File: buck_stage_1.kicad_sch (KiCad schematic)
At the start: 30 parts

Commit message: SH-RPi v2 schematic design
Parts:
- removed C301, C308, C311, C316: (no value), symbol Device:C
- removed R301, R305, R306, R308, R309, R312, R313: (no value), symbol Device:R
- removed U302: (no value), symbol SH-RPi:LMR14050SDDA
- removed U303: (no value), symbol SH-RPi:GS8052
- added C302: 4.7nF, symbol Device:C_Small
- added C304: 100nF, Capacitor_SMD:C_0402_1005Metric, symbol Device:C
- added C305: 100nF, Capacitor_SMD:C_0402_1005Metric, symbol Device:C_Small
- added D301, D304: BZT52C3V3S, Diode_SMD:D_SOD-323, symbol Device:D_Zener
- added D302: 1N4148WT, Diode_SMD:D_SOD-523, symbol Device:D_Small
- added Q301, Q302: MMBT5551, Package_TO_SOT_SMD:SOT-23, symbol Transistor_BJT:MMBT5551L
- added Q303: LBSS84LT1G, Package_TO_SOT_SMD:SOT-23, symbol Transistor_FET:BSS84
- added R302: 576k, Resistor_SMD:R_0402_1005Metric, symbol Device:R
- added R303: 91k, Resistor_SMD:R_0402_1005Metric, symbol Device:R
- added R304: 100k, symbol Device:R
- added R306: 10k, symbol Device:R_Small
- added R309: 18k, symbol Device:R_Small
- added R311: 2k, symbol Device:R
- added U301: RT6365, symbol SH-RPi:RT6365
- added U302, U303: COS1333TRD, Package_TO_SOT_SMD:SOT-23-5, symbol SH-RPi:COS1333
- C301: renamed from C314; value (none) -> 10uF/50V; footprint (none) -> Capacitor_SMD:C_1206_3216Metric; LCSC C13585 -> (none)
- C303: renamed from C304; value (none) -> 100nF; footprint (none) -> Capacitor_SMD:C_0603_1608Metric; LCSC C1525 -> (none)
- C306: value (none) -> 47n; LCSC C15195 -> (none)
- C307: renamed from C305; value (none) -> 47uF/10V; footprint (none) -> Capacitor_SMD:C_0805_2012Metric; LCSC C16780 -> (none); Notes Min 6.3V -> Min 10V
- C308: renamed from C307; value (none) -> 100nF; footprint (none) -> Capacitor_SMD:C_0402_1005Metric
- D303: renamed from D301; value (none) -> SS56; footprint (none) -> Diode_SMD:D_SMA; LCSC C22452 -> C65009
- D305: renamed from D302; value (none) -> 1N4148WT; footprint (none) -> Diode_SMD:D_SOD-523
- JP301: value (none) -> Bridged; footprint (none) -> Jumper:SolderJumper-2_P1.3mm_Bridged_Pad1.0x1.5mm
- L301: value (none) -> FXL0530-3R3-M; footprint (none) -> SH-RPi:L_MWSA0503S; LCSC C285700 -> C475518
- R301: renamed from R304; value (none) -> 50m; footprint (none) -> Resistor_SMD:R_1206_3216Metric; LCSC C127703 -> (none)
- R305: renamed from R311; value (none) -> 68k; footprint (none) -> Resistor_SMD:R_0402_1005Metric; LCSC C25783 -> (none)
- R307: value (none) -> 510R; LCSC C25768 -> (none)
- R308: renamed from R315; value (none) -> 5.1R; footprint (none) -> Resistor_SMD:R_0603_1608Metric
- R310: value (none) -> 100R; LCSC C25918 -> (none)
- R312: renamed from R302; value (none) -> 100k; footprint (none) -> Resistor_SMD:R_0402_1005Metric; LCSC C25774 -> (none)
- R313: renamed from R303; value (none) -> 10k; footprint (none) -> Resistor_SMD:R_0402_1005Metric; LCSC C25750 -> (none)
- R314: value (none) -> 1.1k; LCSC C25769 -> (none)
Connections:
- net EN is gone; now on an unnamed net: R314.1
- net FB: now also U301.5 (FB); no longer C306.2
- net GND: now also C306.1, R307.2, C302.1, C304.1, C305.1, D304.2 (A), Q301.2 (E), R303.1, R311.2, U301.7 (GND), U301.9 (PGND), U303.2 (V-); no longer R310.2, R314.2
- net SW: now also C303.1, U301.8 (SW); no longer R308.1
- net Vin: now also R301.2, R310.1, R310.2, C305.2, D301.1 (K), Q303.2 (S), R304.1, U302.4 (-), U302.5 (V+)
- net Vout: no longer C306.1, R301.2
- net BOOT: now reaches R308.2
- net BOOT: now also U301.1 (BOOT); no longer C303.1
- net at D305.1 (K): now also U303.4 (-); no longer JP301.1 (A)
- net at D305.2 (A): now also U303.1
- net at R307.1: now also Q302.2 (E), R306.2
- net at R305.1: now also U301.4 (RT)
- net BS: no longer names the net of C303.2
- net BS: now also R308.1, D302.1 (K)
- net REG3.3V renamed +3V3
- net +3V3: now also U303.5 (V+)
- net Vcap: no longer names the net of R301.1
- net Vcap: now also R302.1, U301.2 (VIN), U302.3 (+); no longer R307.2
- new net: JP301.1 (A), R314.2
- new net: R302.2, R303.2, U301.3 (EN)
- new net: R309.2, U301.6 (COMP)
- new net: Q303.1 (G), U302.1
- new net: C304.2, D301.2 (A), Q302.3 (C), U302.2 (V-)
- new net: Q301.3 (C), Q302.1 (B), R304.2
- new net: C302.2, R309.1
- new net: Q301.1 (B), R306.1
- new net +5V: D302.2 (A)
- new net Iin: C306.2, D304.1 (K), Q303.3 (D), R311.1, U303.3 (+)
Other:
- note added: "Buck filter design from RT6365 design tool"
- note added: "Constant current source with about 1.25mA current through the biasing zener diode"
- note added: "FB voltage divider designed to have a 8.8V voltage at Vout"
- note added: "Floating opamp with current output. Design from LMP8646."
- note added: "Max 0.8 A current input"
- note added: "Voltage follower with diode rectification"
- note added: "Zener used to protect the next stage from overvoltage"
- note added: "f_sw = 1.393 MHz"
- note removed: "Buck filter design from WEBENCH"
- note removed: "EN voltage divider set to place the UVLO start and stop limits at 8.6 and 7.9V, respectively."
- note removed: "FB voltage divider designed to have a 2.6V voltage at Vout"
- note removed: "Max ca. 3.1 A current output"
- moved on the sheet: C301, C303, C307, C308, D303, D305, JP301, L301, R301, R305, R308, R312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

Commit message: WIP: Assign footprints and LCSC part numbers
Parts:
- added C308: 22uF/16V, Capacitor_SMD:C_0805_2012Metric, symbol Device:C
- C301: LCSC (none) -> C13585
- C302: footprint (none) -> Capacitor_SMD:C_0402_1005Metric; LCSC (none) -> C1538
- C303: LCSC (none) -> C14663
- C306: value 47n -> 47nF; footprint (none) -> Capacitor_SMD:C_0603_1608Metric; LCSC (none) -> C1622
- C307: value 47uF/10V -> 22uF/16V; LCSC (none) -> C98190; Notes Min 10V -> Min 16V
- renumbered C308 to C309
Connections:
- net GND: now also C308.2
- net Vout: now also C308.1
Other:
- moved on the sheet: C307

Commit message: Assign footprints and part numbers to components
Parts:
- removed U303: COS1333TRD, Package_TO_SOT_SMD:SOT-23-5, symbol SH-RPi:COS1333
- added U303: LMV321-TR, Package_TO_SOT_SMD:SOT-23-5, symbol Amplifier_Operational:LMV321
- C306: value 47nF -> 10nF; footprint Capacitor_SMD:C_0603_1608Metric -> Capacitor_SMD:C_0402_1005Metric; LCSC C1622 -> C15195
- R301: value 50m -> 10m; LCSC (none) -> C105362
- R302: value 576k -> 510k; LCSC (none) -> C11616
- R303: value 91k -> 75k; LCSC (none) -> C25798
- R304: footprint (none) -> Resistor_SMD:R_0402_1005Metric; LCSC (none) -> C25741
- R305: LCSC (none) -> C36871
- R306: footprint (none) -> Resistor_SMD:R_0402_1005Metric; LCSC (none) -> C25744
- R307: footprint (none) -> Resistor_SMD:R_0402_1005Metric; LCSC (none) -> C25123
- R309: footprint (none) -> Resistor_SMD:R_0402_1005Metric; LCSC (none) -> C25762
- R310: footprint (none) -> Resistor_SMD:R_0402_1005Metric; LCSC (none) -> C25076
- R311: value 2k -> 10k; footprint (none) -> Resistor_SMD:R_0402_1005Metric; LCSC (none) -> C25744
- R312: LCSC (none) -> C25741
- R313: LCSC (none) -> C25744
- R314: value 1.1k -> 470R; footprint (none) -> Resistor_SMD:R_0402_1005Metric; LCSC (none) -> C25117
- U301: footprint (none) -> Package_SO:SOIC-8-1EP_3.9x4.9mm_P1.27mm_EP2.41x3.3mm_ThermalVias; LCSC (none) -> C3024482
- U302: value COS1333TRD -> COS1333TR; LCSC C5156551 -> C693072
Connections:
- net +3V3: now also U303.5 (V+)
- net GND: now also U303.2 (V-)
- net Iin: now also U303.1 (+)
- net at D305.1 (K), R314.1: now also U303.3 (-)
- net at D305.2 (A): now also U303.4
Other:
- moved on the sheet: C309, R301

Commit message: WIP: PCB layout
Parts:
- added J301: Conn_02x02_Odd_Even, Connector_PinHeader_2.54mm:PinHeader_2x02_P2.54mm_Vertical, symbol Connector_Generic:Conn_02x02_Odd_Even
- added R315: 7.5k, Resistor_SMD:R_0402_1005Metric, symbol Device:R_Small
- added R316: 3.9k, Resistor_SMD:R_0402_1005Metric, symbol Device:R_Small
- D301: LCSC C2932762 -> C188195
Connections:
- net GND: now also R315.2, R316.2
- net Iin: now also J301.1 (Pin_1), J301.3 (Pin_3)
- net Vin: no longer C301.1, Q303.2 (S), R310.2, U302.4 (-)
- net B1_VIN: now reaches R301.1, R302.1, U301.2 (VIN), U302.3 (+)
- net B1_VIN: now also C301.1
- net VF-: now reaches D305.1 (K), R314.1, U303.3 (-)
- net VFO: now reaches D305.2 (A), U303.4
- net FBB: now reaches JP301.1 (A), R314.2
- net CCSE2: now reaches Q302.2 (E), R307.1
- net CCSE2: now also R306.1; no longer R306.2
- net DAO: now reaches Q303.1 (G), U302.1
- net FVSS: now reaches C304.2, D301.2 (A), Q302.3 (C), U302.2 (V-)
- net CCSC1: now reaches Q301.3 (C), Q302.1 (B), R304.2
- net CCSB1: now reaches Q301.1 (B)
- net CCSB1: now also R306.2; no longer R306.1
- new net: J301.2 (Pin_2), R315.1
- new net: J301.4 (Pin_4), R316.1
- new net DA-: Q303.2 (S), R310.2, U302.4 (-)
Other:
- note added: "Current limit adjustment"
- note added: "Place a jumper between 1 and 2 to increase the current limit to 1.9 A."
- note added: "Place a jumper between 3 and 4 to increase the current limit to 2.9 A."
- moved on the sheet: C301, C302, C303, C304, C305, C306, C307, C308, C309, D301, D302, D303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

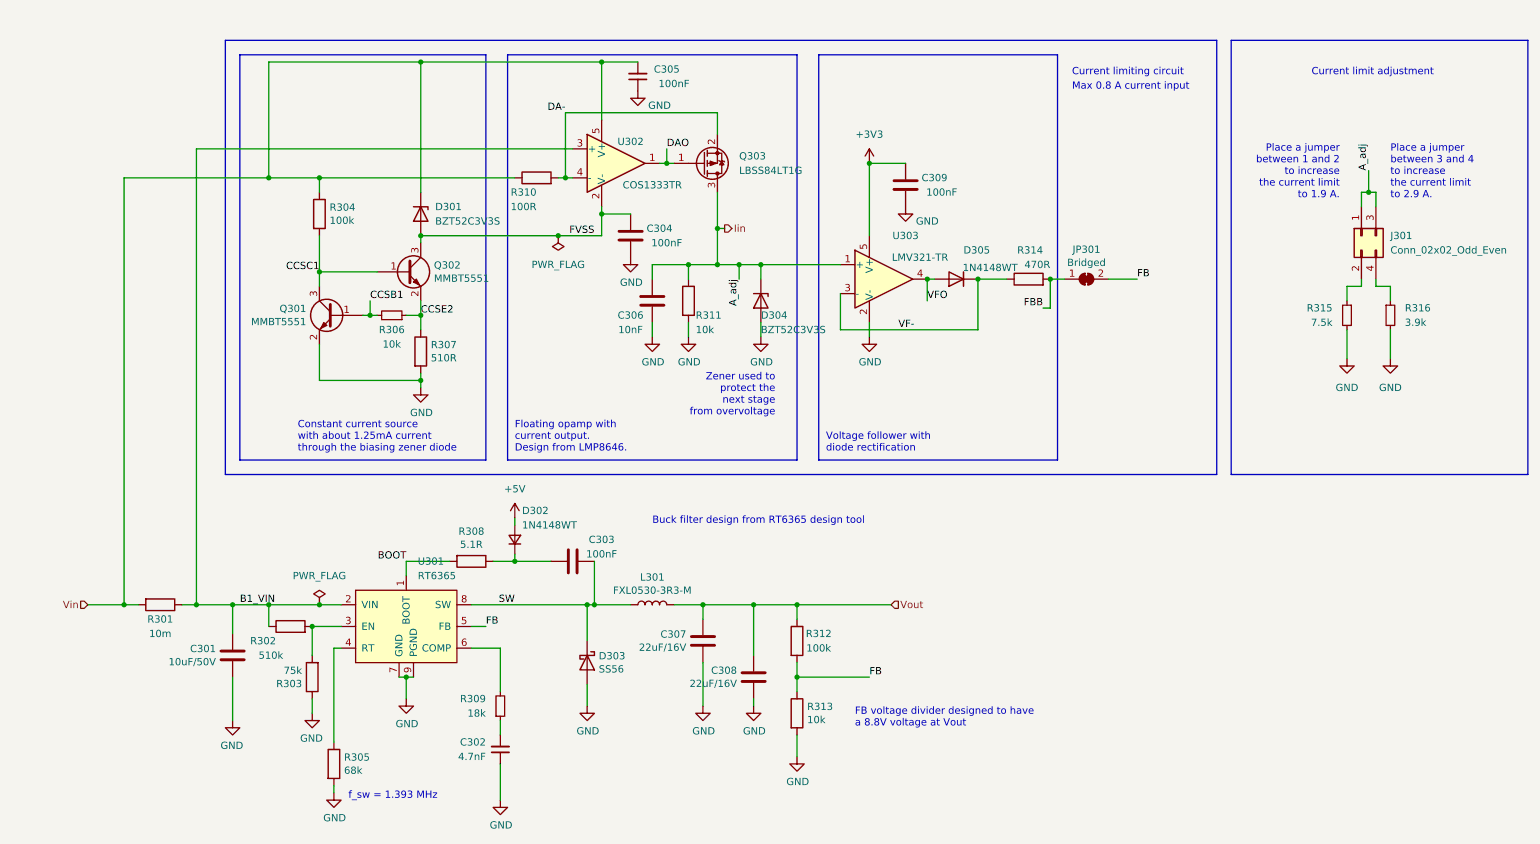
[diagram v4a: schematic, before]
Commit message: Initial PCB component layout done
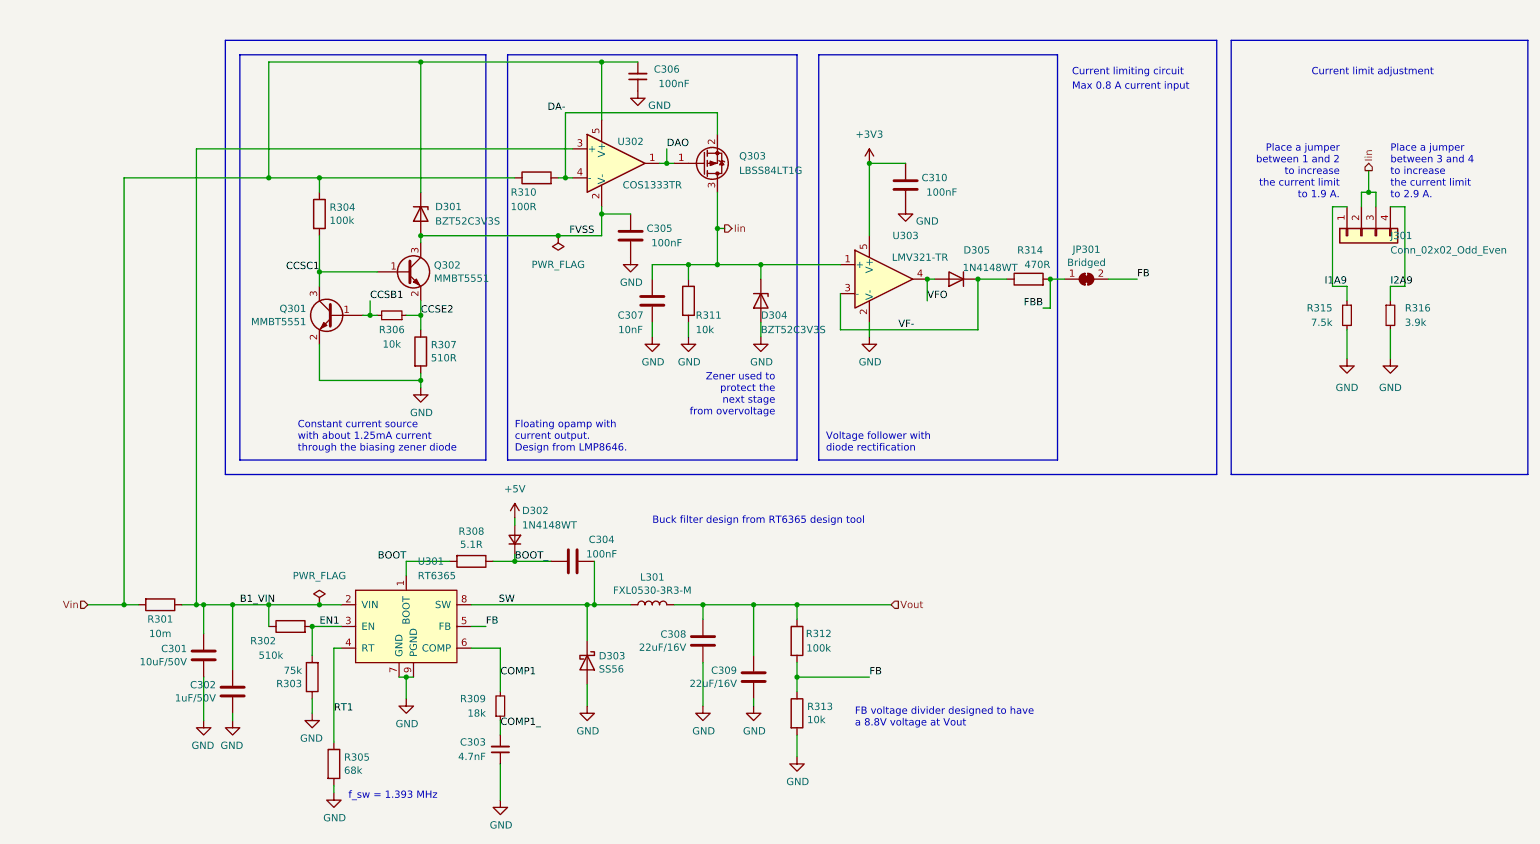
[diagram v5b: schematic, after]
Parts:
- added C302: 1uF/50V, Capacitor_SMD:C_0603_1608Metric, symbol Device:C
- J301: footprint Connector_PinHeader_2.54mm:PinHeader_2x02_P2.54mm_Vertical -> Connector_PinHeader_2.54mm:PinHeader_1x04_P2.54mm_Vertical; symbol Connector_Generic:Conn_02x02_Odd_Even -> Connector_Generic:Conn_01x04
- renumbered C302 to C303, C303 to C304, C304 to C305, C305 to C306, C306 to C307, C307 to C308, C308 to C309, C309 to C310
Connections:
- net B1_VIN: now also C302.1
- net GND: now also C302.2
- net Iin: now also J301.2 (Pin_2); no longer J301.1 (Pin_1)
- net BOOT_: now reaches C304.2, D302.1 (K), R308.1
- net RT1: now reaches R305.1, U301.4 (RT)
- net EN1: now reaches R302.2, R303.2, U301.3 (EN)
- net COMP1: now reaches R309.2, U301.6 (COMP)
- net COMP1_: now reaches C303.2, R309.1
- net I1A9: now reaches R315.1
- net I1A9: now also J301.1 (Pin_1); no longer J301.2 (Pin_2)
- net I2A9: now reaches J301.4 (Pin_4), R316.1
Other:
- moved on the sheet: C301, J301

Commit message: Finish PCB routing
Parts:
- JP301: footprint Jumper:SolderJumper-2_P1.3mm_Bridged_Pad1.0x1.5mm -> Jumper:SolderJumper-2_P1.3mm_Bridged2Bar_RoundedPad1.0x1.5mm
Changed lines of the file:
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@@
     (effects (font (size 1.27 1.27)) (justify right))
   )
-  (hierarchical_label "Vout" (shape input) (at 168.91 121.92 0)
+  (hierarchical_label "Vout" (shape output) (at 168.91 121.92 0)
     (effects (font (size 1.27 1.27)) (justify left))
   )
@@
     (property "Reference" "JP301" (id 0) (at 203.2 59.563 0))
     (property "Value" "Bridged" (id 1) (at 203.2 61.8744 0))
-    (property "Footprint" "Jumper:SolderJumper-2_P1.3mm_Bridged_Pad1.0x1.5mm" (id 2) (at 203.2 64.77 0)
-      (effects (font (size 1.27 1.27)) hide)
-    )
+    (property "Footprint" "Jumper:SolderJumper-2_P1.3mm_Bridged2Bar_RoundedPad1.0x1.5mm" (id 2) (at 203.2 64.77 0)
+      (effects (font (size 1.27 1.27)) hide)
+    )
